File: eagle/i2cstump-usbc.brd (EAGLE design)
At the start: 25.9 x 18.9 mm, 22 parts, among them IC1 ATTINY85, IC2 MCP1703CB, J1 I2C-5V, J2 I2C-3V3, Q1 220mA/50V/3.5Ω, Q2 220mA/50V/3.5Ω

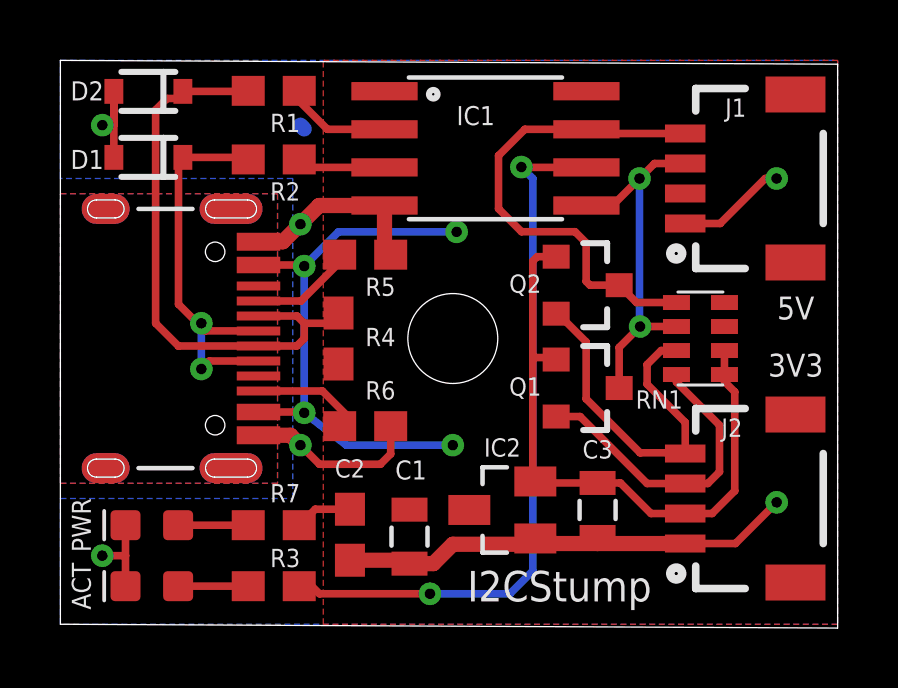
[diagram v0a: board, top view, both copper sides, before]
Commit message: Correct geometry of the v5 board (it was off-by-5mils)
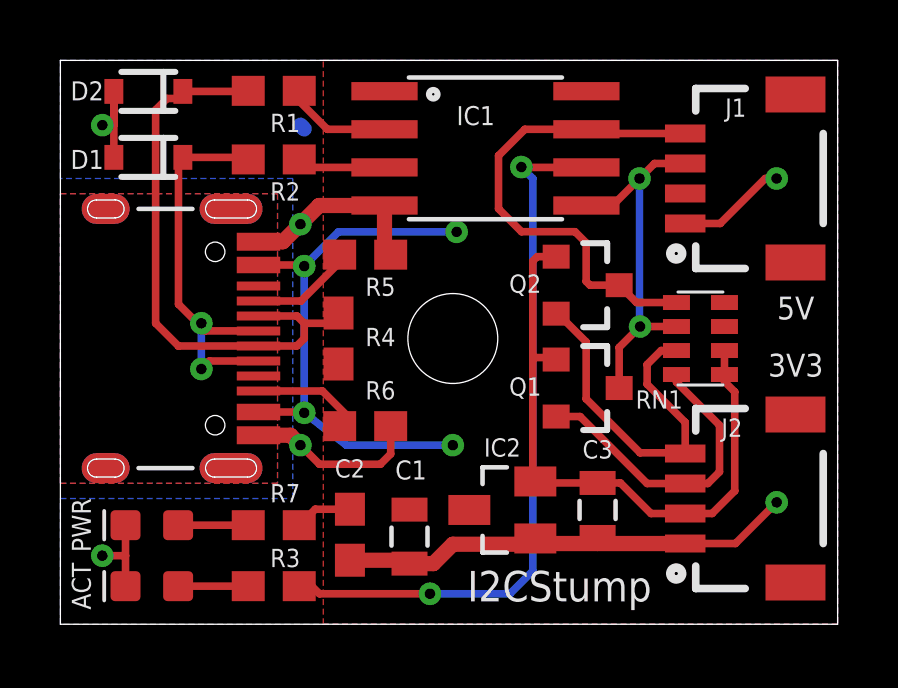
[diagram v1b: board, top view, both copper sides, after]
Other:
- board size 25.9 x 18.9 mm -> 25.9 x 18.8 mm
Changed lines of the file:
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@@
 <drawing>
 <settings>
-<setting alwaysvectorfont="yes"/>
+<setting alwaysvectorfont="no"/>
 <setting keepoldvectorfont="yes"/>
 <setting verticaltext="up"/>
 </settings>
-<grid distance="0.005" unitdist="inch" unit="mil" style="lines" multiple="1" display="yes" altdistance="0.0025" altunitdist="inch" altunit="inch"/>
+<grid distance="0.005" unitdist="inch" unit="mm" style="lines" multiple="1" display="yes" altdistance="0.0025" altunitdist="inch" altunit="inch"/>
 <layers>
 <layer number="1" name="Top" color="4" fill="1" visible="yes" active="yes"/>
@@
 <text x="19.177" y="7.493" size="0.6096" layer="21" font="vector" ratio="25" align="center-left">RN1</text>
 <text x="1.016" y="3.302" size="0.635" layer="21" font="vector" ratio="20" distance="80" rot="R90" align="bottom-center">PWR</text>
-<wire x1="0" y1="0" x2="25.908" y2="-0.127" width="0.0254" layer="20"/>
-<wire x1="25.908" y1="-0.127" x2="25.908" y2="18.669" width="0.0254" layer="20"/>
-<wire x1="25.908" y1="18.669" x2="0" y2="18.796" width="0.0254" layer="20"/>
+<wire x1="0" y1="0" x2="25.908" y2="0" width="0.0254" layer="20"/>
+<wire x1="25.908" y1="0" x2="25.908" y2="18.796" width="0.0254" layer="20"/>
+<wire x1="25.908" y1="18.796" x2="0" y2="18.796" width="0.0254" layer="20"/>
 <wire x1="0" y1="18.796" x2="0" y2="0" width="0.0254" layer="20"/>
 </plain>

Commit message: Center the USB-C connector
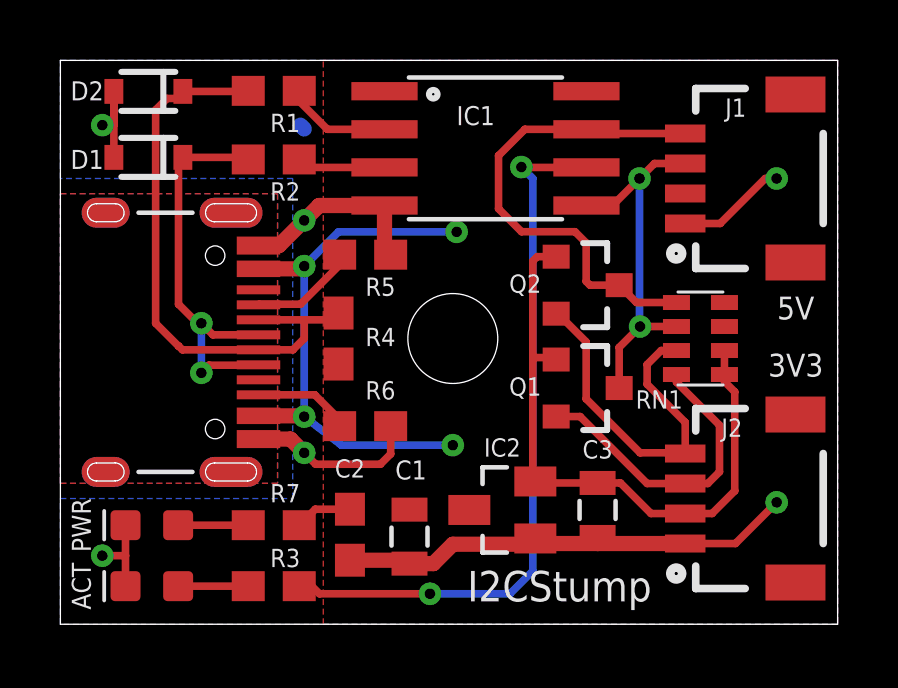
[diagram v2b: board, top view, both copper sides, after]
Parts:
- moved J3 0.13 mm to (6.60, 9.40)
